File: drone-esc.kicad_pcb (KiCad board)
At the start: 4 copper layers, 30 x 30 mm, 0 parts

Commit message: added board footprint
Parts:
- added C1: 100n, Capacitor_SMD:C_0201_0603Metric, B.Cu at (140.5, 118.2)
- added C10: 10u, Capacitor_SMD:C_0805_2012Metric, B.Cu at (157.3, 124.8)
- added C11: 10u, Capacitor_SMD:C_0805_2012Metric, B.Cu at (157.3, 127.8)
- added C12: 10u, Capacitor_SMD:C_0805_2012Metric, B.Cu at (152.8, 118.8)
- added C13: 10u, Capacitor_SMD:C_0805_2012Metric, B.Cu at (152.8, 121.8)
- added C14: 10u, Capacitor_SMD:C_0805_2012Metric, B.Cu at (152.8, 124.8)
- added C15: 10u, Capacitor_SMD:C_0805_2012Metric, B.Cu at (152.8, 127.8)
- added C16: 10u, Capacitor_SMD:C_0805_2012Metric, B.Cu at (148.4, 118.8)
- added C17: 10u, Capacitor_SMD:C_0805_2012Metric, B.Cu at (148.4, 121.8)
- added C18: 10u, Capacitor_SMD:C_0805_2012Metric, B.Cu at (148.4, 124.8)
- added C19: 10u, Capacitor_SMD:C_0805_2012Metric, B.Cu at (148.4, 127.8)
- added C2: 100n, Capacitor_SMD:C_0201_0603Metric, B.Cu at (140.5, 119.9)
- added C20: 10u, Capacitor_SMD:C_0805_2012Metric, B.Cu at (143.9, 118.8)
- added C21: 10u, Capacitor_SMD:C_0805_2012Metric, B.Cu at (143.9, 121.8)
- added C22: 10u, Capacitor_SMD:C_0805_2012Metric, B.Cu at (143.9, 124.8)
- added C23: 10u, Capacitor_SMD:C_0805_2012Metric, B.Cu at (143.9, 127.8)
- added C25: 100n, Capacitor_SMD:C_0201_0603Metric, F.Cu at (104.3, 43.2)
- added C26: 100n, Capacitor_SMD:C_0201_0603Metric, F.Cu at (104.3, 45.0)
- added C27: 100n, Capacitor_SMD:C_0201_0603Metric, F.Cu at (104.3, 46.7)
- added C28: 100n, Capacitor_SMD:C_0201_0603Metric, F.Cu at (181.7, 42.9)
- added C29: 100n, Capacitor_SMD:C_0201_0603Metric, F.Cu at (104.3, 48.5)
- added C3: 1u, Capacitor_SMD:C_0201_0603Metric, B.Cu at (140.5, 121.7)
- added C30: 100n, Capacitor_SMD:C_0201_0603Metric, F.Cu at (104.3, 50.2)
- added C31: 100n, Capacitor_SMD:C_0201_0603Metric, F.Cu at (104.3, 52.0)
- added C32: 100n, Capacitor_SMD:C_0201_0603Metric, F.Cu at (104.3, 53.7)
- added C33: 100n, Capacitor_SMD:C_0201_0603Metric, F.Cu at (83.0, 111.8)
- added C34: 100n, Capacitor_SMD:C_0201_0603Metric, F.Cu at (83.0, 113.5)
- added C35: 100n, Capacitor_SMD:C_0201_0603Metric, F.Cu at (83.0, 115.3)
- added C36: 100n, Capacitor_SMD:C_0201_0603Metric, F.Cu at (83.0, 117.0)
- added C37: 100n, Capacitor_SMD:C_0201_0603Metric, F.Cu at (83.0, 118.8)
- added C38: 100n, Capacitor_SMD:C_0201_0603Metric, F.Cu at (83.0, 120.5)
- added C39: 100n, Capacitor_SMD:C_0201_0603Metric, F.Cu at (83.0, 122.3)
- added C4: 2u2, Capacitor_SMD:C_0201_0603Metric, B.Cu at (140.5, 123.4)
- added C40: 100n, Capacitor_SMD:C_0201_0603Metric, F.Cu at (83.0, 124.0)
- added C41: 100n, Capacitor_SMD:C_0201_0603Metric, F.Cu at (85.4, 111.8)
- added C42: 100n, Capacitor_SMD:C_0201_0603Metric, F.Cu at (104.3, 55.5)
- added C43: 100n, Capacitor_SMD:C_0201_0603Metric, F.Cu at (181.7, 44.6)
- added C44: 100n, Capacitor_SMD:C_0201_0603Metric, F.Cu at (181.7, 46.4)
- added C45: 100n, Capacitor_SMD:C_0201_0603Metric, F.Cu at (106.7, 43.2)
- added C46: 100n, Capacitor_SMD:C_0201_0603Metric, F.Cu at (181.7, 48.1)
- added C47: 100n, Capacitor_SMD:C_0201_0603Metric, F.Cu at (181.7, 49.9)
- added C48: 100n, Capacitor_SMD:C_0201_0603Metric, F.Cu at (181.7, 51.6)
- added C49: 100n, Capacitor_SMD:C_0201_0603Metric, F.Cu at (181.7, 53.4)
- added C5: 22u, Capacitor_SMD:C_0201_0603Metric, B.Cu at (138.0, 118.2)
- added C50: 100n, Capacitor_SMD:C_0201_0603Metric, F.Cu at (181.7, 55.1)
- added C51: 100n, Capacitor_SMD:C_0201_0603Metric, F.Cu at (184.2, 42.9)
- added C52: 100n, Capacitor_SMD:C_0201_0603Metric, F.Cu at (190.4, 111.1)
- added C53: 100n, Capacitor_SMD:C_0201_0603Metric, F.Cu at (190.4, 112.8)
- added C54: 100n, Capacitor_SMD:C_0201_0603Metric, F.Cu at (190.4, 114.6)
- added C55: 100n, Capacitor_SMD:C_0201_0603Metric, F.Cu at (190.4, 116.3)
- added C56: 100n, Capacitor_SMD:C_0201_0603Metric, F.Cu at (190.4, 118.1)
- added C57: 100n, Capacitor_SMD:C_0201_0603Metric, F.Cu at (190.4, 119.8)
- added C58: 100n, Capacitor_SMD:C_0201_0603Metric, F.Cu at (190.4, 121.6)
- added C59: 100n, Capacitor_SMD:C_0201_0603Metric, F.Cu at (190.4, 123.3)
- added C6: 10u, Capacitor_SMD:C_0201_0603Metric, B.Cu at (138.0, 119.9)
- added C60: 100n, Capacitor_SMD:C_0201_0603Metric, F.Cu at (192.9, 111.1)
- added C7: 22u, Capacitor_SMD:C_0201_0603Metric, B.Cu at (138.0, 121.7)
- added C8: 10u, Capacitor_SMD:C_0805_2012Metric, B.Cu at (157.3, 118.8)
- added C9: 10u, Capacitor_SMD:C_0805_2012Metric, B.Cu at (157.3, 121.8)
- added D1: SMF5.0A, Diode_SMD:D_SOD-123F, B.Cu at (141.9, 146.8)
- added D1: SMF5.0A, Diode_SMD:D_SOD-123F, B.Cu at (138.9, 126.0)
- added D2: HSMG-C170, LED_SMD:LED_0805_2012Metric, B.Cu at (136.3, 130.9)
- added D3: HSMD-C170, LED_SMD:LED_0805_2012Metric, B.Cu at (136.3, 133.9)
- added D4: HSMG-C170, LED_SMD:LED_0805_2012Metric, F.Cu at (114.4, 64.1)
- added D5: HSMG-C170, LED_SMD:LED_0805_2012Metric, F.Cu at (93.1, 132.7)
- added D6: HSMG-C170, LED_SMD:LED_0805_2012Metric, F.Cu at (191.9, 63.8)
- added D7: HSMG-C170, LED_SMD:LED_0805_2012Metric, F.Cu at (200.6, 132.0)
- added FB1: BLM03HD331SN1D, Resistor_SMD:R_0201_0603Metric, F.Cu at (106.7, 45.0)
- added FB2: BLM03HD331SN1D, Resistor_SMD:R_0201_0603Metric, F.Cu at (85.4, 113.5)
- added FB3: BLM03HD331SN1D, Resistor_SMD:R_0201_0603Metric, F.Cu at (184.2, 44.6)
- added FB4: BLM03HD331SN1D, Resistor_SMD:R_0201_0603Metric, F.Cu at (192.9, 112.8)
- added J1: SM08B-SRSS-TB_LF__SN_, SM08B-SRSS-TB:JST_SM08B-SRSS-TB_LF__SN_, B.Cu at (145.1, 80.2)
- added L1: 1u, Inductor_SMD:L_0603_1608Metric, B.Cu at (136.5, 136.7)
- added Q1: IRLHS6242, IRLHS6242TRPBF:IRL100HS121-V, F.Cu at (100.6, 44.6)
- added Q10: IRLHS6242, IRLHS6242TRPBF:IRL100HS121-V, F.Cu at (79.3, 127.1)
- added Q11: IRLHS6242, IRLHS6242TRPBF:IRL100HS121-V, F.Cu at (79.3, 131.7)
- added Q12: IRLHS6242, IRLHS6242TRPBF:IRL100HS121-V, F.Cu at (79.3, 136.3)
- added Q13: IRLHS6242, IRLHS6242TRPBF:IRL100HS121-V, F.Cu at (178.0, 44.3)
- added Q14: IRLHS6242, IRLHS6242TRPBF:IRL100HS121-V, F.Cu at (178.0, 49.0)
- added Q15: IRLHS6242, IRLHS6242TRPBF:IRL100HS121-V, F.Cu at (178.0, 53.6)
- added Q16: IRLHS6242, IRLHS6242TRPBF:IRL100HS121-V, F.Cu at (178.0, 58.2)
- added Q17: IRLHS6242, IRLHS6242TRPBF:IRL100HS121-V, F.Cu at (178.0, 62.8)
- added Q18: IRLHS6242, IRLHS6242TRPBF:IRL100HS121-V, F.Cu at (178.0, 67.4)
- added Q19: IRLHS6242, IRLHS6242TRPBF:IRL100HS121-V, F.Cu at (186.7, 112.5)
- added Q2: IRLHS6242, IRLHS6242TRPBF:IRL100HS121-V, F.Cu at (100.6, 49.3)
- added Q20: IRLHS6242, IRLHS6242TRPBF:IRL100HS121-V, F.Cu at (186.7, 117.2)
- added Q21: IRLHS6242, IRLHS6242TRPBF:IRL100HS121-V, F.Cu at (186.7, 121.8)
- added Q22: IRLHS6242, IRLHS6242TRPBF:IRL100HS121-V, F.Cu at (186.7, 126.4)
- added Q23: IRLHS6242, IRLHS6242TRPBF:IRL100HS121-V, F.Cu at (186.7, 131.0)
- added Q24: IRLHS6242, IRLHS6242TRPBF:IRL100HS121-V, F.Cu at (186.7, 135.6)
- added Q3: IRLHS6242, IRLHS6242TRPBF:IRL100HS121-V, F.Cu at (100.6, 53.9)
- added Q4: IRLHS6242, IRLHS6242TRPBF:IRL100HS121-V, F.Cu at (100.6, 58.5)
- added Q5: IRLHS6242, IRLHS6242TRPBF:IRL100HS121-V, F.Cu at (100.6, 63.1)
- added Q6: IRLHS6242, IRLHS6242TRPBF:IRL100HS121-V, F.Cu at (100.6, 67.7)
- added Q7: IRLHS6242, IRLHS6242TRPBF:IRL100HS121-V, F.Cu at (79.3, 113.2)
- added Q8: IRLHS6242, IRLHS6242TRPBF:IRL100HS121-V, F.Cu at (79.3, 117.9)
- added Q9: IRLHS6242, IRLHS6242TRPBF:IRL100HS121-V, F.Cu at (79.3, 122.5)
- added R1: 1m, Resistor_SMD:R_2512_6332Metric, B.Cu at (142.9, 131.8)
- added R10: 100k, Resistor_SMD:R_0201_0603Metric, F.Cu at (106.7, 53.7)
- added R11: 100k, Resistor_SMD:R_0201_0603Metric, F.Cu at (184.2, 46.4)
- added R12: 15R, Resistor_SMD:R_0201_0603Metric, F.Cu at (106.7, 55.5)
- added R13: 15R, Resistor_SMD:R_0201_0603Metric, F.Cu at (109.2, 43.2)
- added R14: 15R, Resistor_SMD:R_0201_0603Metric, F.Cu at (109.2, 45.0)
- added R15: 15R, Resistor_SMD:R_0201_0603Metric, F.Cu at (109.2, 46.7)
- added R16: 15R, Resistor_SMD:R_0201_0603Metric, F.Cu at (109.2, 48.5)
- added R17: 4.7k, Resistor_SMD:R_0201_0603Metric, F.Cu at (109.2, 50.2)
- added R18: 1k, Resistor_SMD:R_0201_0603Metric, F.Cu at (109.2, 52.0)
- added R19: 10k, Resistor_SMD:R_0201_0603Metric, F.Cu at (109.2, 53.7)
- added R2: 1k, Resistor_SMD:R_0201_0603Metric, B.Cu at (142.9, 136.7)
- added R20: 4.7k, Resistor_SMD:R_0201_0603Metric, F.Cu at (109.2, 55.5)
- added R21: 10k, Resistor_SMD:R_0201_0603Metric, F.Cu at (111.6, 43.2)
- added R22: 1k, Resistor_SMD:R_0201_0603Metric, F.Cu at (111.6, 45.0)
- added R23: 4.7k, Resistor_SMD:R_0201_0603Metric, F.Cu at (111.6, 46.7)
- added R24: 10k, Resistor_SMD:R_0201_0603Metric, F.Cu at (111.6, 48.5)
- added R25: 1k, Resistor_SMD:R_0201_0603Metric, F.Cu at (111.6, 50.2)
- added R26: 10k, Resistor_SMD:R_0201_0603Metric, F.Cu at (85.4, 115.3)
- added R27: 100k, Resistor_SMD:R_0201_0603Metric, F.Cu at (85.4, 117.0)
- added R28: 100k, Resistor_SMD:R_0201_0603Metric, F.Cu at (85.4, 118.8)
- added R29: 100k, Resistor_SMD:R_0201_0603Metric, F.Cu at (85.4, 120.5)
- added R3: 732k, Resistor_SMD:R_0201_0603Metric, B.Cu at (138.0, 123.4)
- added R30: 10k, Resistor_SMD:R_0201_0603Metric, F.Cu at (85.4, 122.3)
- added R31: 220R, Resistor_SMD:R_0201_0603Metric, F.Cu at (85.4, 124.0)
- added R32: 15R, Resistor_SMD:R_0201_0603Metric, F.Cu at (87.9, 111.8)
- added R33: 15R, Resistor_SMD:R_0201_0603Metric, F.Cu at (87.9, 113.5)
- added R34: 4.7k, Resistor_SMD:R_0201_0603Metric, F.Cu at (87.9, 115.3)
- added R35: 10k, Resistor_SMD:R_0201_0603Metric, F.Cu at (87.9, 117.0)
- added R36: 15R, Resistor_SMD:R_0201_0603Metric, F.Cu at (87.9, 118.8)
- added R37: 15R, Resistor_SMD:R_0201_0603Metric, F.Cu at (87.9, 120.5)
- added R38: 1k, Resistor_SMD:R_0201_0603Metric, F.Cu at (87.9, 122.3)
- added R39: 4.7k, Resistor_SMD:R_0201_0603Metric, F.Cu at (87.9, 124.0)
- added R4: 100k, Resistor_SMD:R_0201_0603Metric, B.Cu at (135.6, 118.2)
- added R40: 10k, Resistor_SMD:R_0201_0603Metric, F.Cu at (90.3, 111.8)
- added R41: 1k, Resistor_SMD:R_0201_0603Metric, F.Cu at (90.3, 113.5)
- added R42: 15R, Resistor_SMD:R_0201_0603Metric, F.Cu at (90.3, 115.3)
- added R43: 15R, Resistor_SMD:R_0201_0603Metric, F.Cu at (90.3, 117.0)
- added R44: 4.7k, Resistor_SMD:R_0201_0603Metric, F.Cu at (90.3, 118.8)
- added R45: 10k, Resistor_SMD:R_0201_0603Metric, F.Cu at (90.3, 120.5)
- added R46: 1k, Resistor_SMD:R_0201_0603Metric, F.Cu at (90.3, 122.3)
- added R47: 10k, Resistor_SMD:R_0201_0603Metric, F.Cu at (111.6, 52.0)
- added R48: 10k, Resistor_SMD:R_0201_0603Metric, F.Cu at (184.2, 48.1)
- added R49: 100k, Resistor_SMD:R_0201_0603Metric, F.Cu at (184.2, 49.9)
- added R5: 360, Resistor_SMD:R_0201_0603Metric, B.Cu at (135.6, 119.9)
- added R50: 100k, Resistor_SMD:R_0201_0603Metric, F.Cu at (184.2, 51.6)
- added R51: 10k, Resistor_SMD:R_0201_0603Metric, F.Cu at (184.2, 53.4)
- added R52: 220R, Resistor_SMD:R_0201_0603Metric, F.Cu at (184.2, 55.1)
- added R53: 15R, Resistor_SMD:R_0201_0603Metric, F.Cu at (111.6, 53.7)
- added R54: 15R, Resistor_SMD:R_0201_0603Metric, F.Cu at (186.6, 42.9)
- added R55: 15R, Resistor_SMD:R_0201_0603Metric, F.Cu at (186.6, 44.6)
- added R56: 4.7k, Resistor_SMD:R_0201_0603Metric, F.Cu at (186.6, 46.4)
- added R57: 10k, Resistor_SMD:R_0201_0603Metric, F.Cu at (186.6, 48.1)
- added R58: 15R, Resistor_SMD:R_0201_0603Metric, F.Cu at (186.6, 49.9)
- added R59: 15R, Resistor_SMD:R_0201_0603Metric, F.Cu at (186.6, 51.6)
- added R6: 10k, Resistor_SMD:R_0201_0603Metric, F.Cu at (106.7, 46.7)
- added R60: 1k, Resistor_SMD:R_0201_0603Metric, F.Cu at (186.6, 53.4)
- added R61: 4.7k, Resistor_SMD:R_0201_0603Metric, F.Cu at (186.6, 55.1)
- added R62: 10k, Resistor_SMD:R_0201_0603Metric, F.Cu at (189.1, 42.9)
- added R63: 1k, Resistor_SMD:R_0201_0603Metric, F.Cu at (189.1, 44.6)
- added R64: 15R, Resistor_SMD:R_0201_0603Metric, F.Cu at (189.1, 46.4)
- added R65: 15R, Resistor_SMD:R_0201_0603Metric, F.Cu at (189.1, 48.1)
- added R66: 4.7k, Resistor_SMD:R_0201_0603Metric, F.Cu at (189.1, 49.9)
- added R67: 10k, Resistor_SMD:R_0201_0603Metric, F.Cu at (189.1, 51.6)
- added R68: 1k, Resistor_SMD:R_0201_0603Metric, F.Cu at (189.1, 53.4)
- added R69: 10k, Resistor_SMD:R_0201_0603Metric, F.Cu at (192.9, 114.6)
- added R7: 220R, Resistor_SMD:R_0201_0603Metric, F.Cu at (106.7, 48.5)
- added R70: 100k, Resistor_SMD:R_0201_0603Metric, F.Cu at (192.9, 116.3)
- added R71: 100k, Resistor_SMD:R_0201_0603Metric, F.Cu at (192.9, 118.1)
- added R72: 100k, Resistor_SMD:R_0201_0603Metric, F.Cu at (192.9, 119.8)
- added R73: 10k, Resistor_SMD:R_0201_0603Metric, F.Cu at (192.9, 121.6)
- added R74: 220R, Resistor_SMD:R_0201_0603Metric, F.Cu at (192.9, 123.3)
- added R75: 15R, Resistor_SMD:R_0201_0603Metric, F.Cu at (195.3, 111.1)
- added R76: 15R, Resistor_SMD:R_0201_0603Metric, F.Cu at (195.3, 112.8)
- added R77: 4.7k, Resistor_SMD:R_0201_0603Metric, F.Cu at (195.3, 114.6)
- added R78: 10k, Resistor_SMD:R_0201_0603Metric, F.Cu at (195.3, 116.3)
- added R79: 15R, Resistor_SMD:R_0201_0603Metric, F.Cu at (195.3, 118.1)
- added R8: 100k, Resistor_SMD:R_0201_0603Metric, F.Cu at (106.7, 50.2)
- added R80: 15R, Resistor_SMD:R_0201_0603Metric, F.Cu at (195.3, 119.8)
- added R81: 1k, Resistor_SMD:R_0201_0603Metric, F.Cu at (195.3, 121.6)
- added R82: 4.7k, Resistor_SMD:R_0201_0603Metric, F.Cu at (195.3, 123.3)
- added R83: 10k, Resistor_SMD:R_0201_0603Metric, F.Cu at (197.8, 111.1)
- added R84: 1k, Resistor_SMD:R_0201_0603Metric, F.Cu at (197.8, 112.8)
- added R85: 15R, Resistor_SMD:R_0201_0603Metric, F.Cu at (197.8, 114.6)
- added R86: 15R, Resistor_SMD:R_0201_0603Metric, F.Cu at (197.8, 116.3)
- added R87: 4.7k, Resistor_SMD:R_0201_0603Metric, F.Cu at (197.8, 118.1)
- added R88: 10k, Resistor_SMD:R_0201_0603Metric, F.Cu at (197.8, 119.8)
- added R89: 1k, Resistor_SMD:R_0201_0603Metric, F.Cu at (197.8, 121.6)
- added R9: 100k, Resistor_SMD:R_0201_0603Metric, F.Cu at (106.7, 52.0)
- added R90: 900, Resistor_SMD:R_0201_0603Metric, B.Cu at (135.6, 121.7)
- added R91: 360, Resistor_SMD:R_0201_0603Metric, F.Cu at (111.6, 55.5)
- added R92: 360, Resistor_SMD:R_0201_0603Metric, F.Cu at (90.3, 124.0)
- added R93: 360, Resistor_SMD:R_0201_0603Metric, F.Cu at (189.1, 55.1)
- added R94: 360, Resistor_SMD:R_0201_0603Metric, F.Cu at (197.8, 123.3)
- added TP10: SWDIO, TestPoint:TestPoint_Pad_D1.0mm, F.Cu at (182.0, 63.6)
- added TP11: NRST, TestPoint:TestPoint_Pad_D1.0mm, F.Cu at (190.7, 125.8)
- added TP12: SWCLK, TestPoint:TestPoint_Pad_D1.0mm, F.Cu at (190.7, 128.8)
- added TP13: SWDIO, TestPoint:TestPoint_Pad_D1.0mm, F.Cu at (190.7, 131.8)
- added TP14: BATT, TestPoint:TestPoint_Pad_D1.0mm, B.Cu at (158.0, 136.1)
- added TP15: GND, TestPoint:TestPoint_Pad_D1.0mm, B.Cu at (158.0, 141.0)
- added TP16: 3V3, TestPoint:TestPoint_Pad_D1.0mm, B.Cu at (154.9, 136.1)
- added TP17: 5V, TestPoint:TestPoint_Pad_D1.0mm, B.Cu at (154.9, 141.0)
- added TP18: CURR, TestPoint:TestPoint_Pad_D1.0mm, B.Cu at (151.9, 136.1)
- added TP19: BOOT0, TestPoint:TestPoint_Pad_D1.0mm, F.Cu at (107.6, 57.9)
- added TP2: SWCLK, TestPoint:TestPoint_Pad_D1.0mm, F.Cu at (104.6, 57.9)
- added TP20: BOOT0, TestPoint:TestPoint_Pad_D1.0mm, F.Cu at (86.3, 126.5)
- added TP21: BOOT0, TestPoint:TestPoint_Pad_D1.0mm, F.Cu at (185.1, 57.5)
- added TP22: BOOT0, TestPoint:TestPoint_Pad_D1.0mm, F.Cu at (193.8, 125.8)
- added TP23: GND, TestPoint:TestPoint_Pad_D1.0mm, B.Cu at (151.9, 141.0)
- added TP24: GAH, TestPoint:TestPoint_Pad_D1.0mm, F.Cu at (107.6, 60.9)
- added TP25: GAH, TestPoint:TestPoint_Pad_D1.0mm, F.Cu at (86.3, 129.5)
- added TP26: GAH, TestPoint:TestPoint_Pad_D1.0mm, F.Cu at (185.1, 60.6)
- added TP27: GAH, TestPoint:TestPoint_Pad_D1.0mm, F.Cu at (193.8, 128.8)
- added TP3: NRST, TestPoint:TestPoint_Pad_D1.0mm, F.Cu at (104.6, 60.9)
- added TP36: GAL, TestPoint:TestPoint_Pad_D1.0mm, F.Cu at (107.6, 64.0)
- added TP37: GAL, TestPoint:TestPoint_Pad_D1.0mm, F.Cu at (86.3, 132.6)
- added TP38: GAL, TestPoint:TestPoint_Pad_D1.0mm, F.Cu at (185.1, 63.6)
- added TP39: GAL, TestPoint:TestPoint_Pad_D1.0mm, F.Cu at (193.8, 131.8)
- added TP4: NRST, TestPoint:TestPoint_Pad_D1.0mm, F.Cu at (83.3, 126.5)
- added TP48: MOTORA, TestPoint:TestPoint_Pad_D1.0mm, F.Cu at (110.7, 57.9)
- added TP49: MOTORA, TestPoint:TestPoint_Pad_D1.0mm, F.Cu at (89.4, 126.5)
- added TP5: SWCLK, TestPoint:TestPoint_Pad_D1.0mm, F.Cu at (83.3, 129.5)
- added TP50: MOTORA, TestPoint:TestPoint_Pad_D1.0mm, F.Cu at (188.1, 57.5)
- added TP51: MOTORA, TestPoint:TestPoint_Pad_D1.0mm, F.Cu at (196.8, 125.8)
- added TP52: MOTORB, TestPoint:TestPoint_Pad_D1.0mm, F.Cu at (110.7, 60.9)
- added TP53: MOTORB, TestPoint:TestPoint_Pad_D1.0mm, F.Cu at (89.4, 129.5)
- added TP54: MOTORB, TestPoint:TestPoint_Pad_D1.0mm, F.Cu at (188.1, 60.6)
- added TP55: MOTORB, TestPoint:TestPoint_Pad_D1.0mm, F.Cu at (196.8, 128.8)
- added TP56: MOTORC, TestPoint:TestPoint_Pad_D1.0mm, F.Cu at (110.7, 64.0)
- added TP57: MOTORC, TestPoint:TestPoint_Pad_D1.0mm, F.Cu at (89.4, 132.6)
- added TP58: MOTORC, TestPoint:TestPoint_Pad_D1.0mm, F.Cu at (188.1, 63.6)
- added TP59: MOTORC, TestPoint:TestPoint_Pad_D1.0mm, F.Cu at (196.8, 131.8)
- added TP6: SWDIO, TestPoint:TestPoint_Pad_D1.0mm, F.Cu at (83.3, 132.6)
- added TP7: NRST, TestPoint:TestPoint_Pad_D1.0mm, F.Cu at (182.0, 57.5)
- added TP8: SWCLK, TestPoint:TestPoint_Pad_D1.0mm, F.Cu at (182.0, 60.6)
- added TP9: SWDIO, TestPoint:TestPoint_Pad_D1.0mm, F.Cu at (104.6, 64.0)
- added U1: ~, esc-board-copper:esc-board, F.Cu at (145.0, 95.0)
- added U10: DGD05473FNQ-7, Package_DFN_QFN:DFN-10-1EP_3x3mm_P0.5mm_EP1.7x2.5mm, F.Cu at (94.6, 117.8)
- added U11: DGD05473FNQ-7, Package_DFN_QFN:DFN-10-1EP_3x3mm_P0.5mm_EP1.7x2.5mm, F.Cu at (94.6, 122.3)
- added U12: AT32F421G8U7, Package_DFN_QFN:QFN-28-1EP_4x4mm_P0.45mm_EP2.4x2.4mm, F.Cu at (94.4, 128.1)
- added U13: DGD05473FNQ-7, Package_DFN_QFN:DFN-10-1EP_3x3mm_P0.5mm_EP1.7x2.5mm, F.Cu at (193.3, 44.3)
- added U14: DGD05473FNQ-7, Package_DFN_QFN:DFN-10-1EP_3x3mm_P0.5mm_EP1.7x2.5mm, F.Cu at (193.3, 48.9)
- added U15: DGD05473FNQ-7, Package_DFN_QFN:DFN-10-1EP_3x3mm_P0.5mm_EP1.7x2.5mm, F.Cu at (193.3, 53.4)
- added U16: AT32F421G8U7, Package_DFN_QFN:QFN-28-1EP_4x4mm_P0.45mm_EP2.4x2.4mm, F.Cu at (193.1, 59.1)
- added U17: DGD05473FNQ-7, Package_DFN_QFN:DFN-10-1EP_3x3mm_P0.5mm_EP1.7x2.5mm, F.Cu at (202.0, 112.5)
- added U18: DGD05473FNQ-7, Package_DFN_QFN:DFN-10-1EP_3x3mm_P0.5mm_EP1.7x2.5mm, F.Cu at (202.0, 117.0)
- added U19: DGD05473FNQ-7, Package_DFN_QFN:DFN-10-1EP_3x3mm_P0.5mm_EP1.7x2.5mm, F.Cu at (202.0, 121.6)
- added U2: INA186A3IDCKR, INA186A3IDCKR:SOT65P210X110-6N, B.Cu at (144.4, 140.9)
- added U20: AT32F421G8U7, Package_DFN_QFN:QFN-28-1EP_4x4mm_P0.45mm_EP2.4x2.4mm, F.Cu at (201.8, 127.3)
- added U3: TLV76733DRVR, Package_SON:WSON-6-1EP_2x2mm_P0.65mm_EP1x1.6mm_ThermalVias, B.Cu at (136.7, 139.8)
- added U4: TPS61023DRLR, TPS61023DRLR:DRL0006A, B.Cu at (139.8, 139.5)
- added U5: AT32F421G8U7, Package_DFN_QFN:QFN-28-1EP_4x4mm_P0.45mm_EP2.4x2.4mm, F.Cu at (115.7, 59.5)
- added U6: DGD05473FNQ-7, Package_DFN_QFN:DFN-10-1EP_3x3mm_P0.5mm_EP1.7x2.5mm, F.Cu at (115.9, 44.6)
- added U7: DGD05473FNQ-7, Package_DFN_QFN:DFN-10-1EP_3x3mm_P0.5mm_EP1.7x2.5mm, F.Cu at (115.9, 49.1)
- added U8: DGD05473FNQ-7, Package_DFN_QFN:DFN-10-1EP_3x3mm_P0.5mm_EP1.7x2.5mm, F.Cu at (115.9, 53.7)
- added U9: DGD05473FNQ-7, Package_DFN_QFN:DFN-10-1EP_3x3mm_P0.5mm_EP1.7x2.5mm, F.Cu at (94.6, 113.2)
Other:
- outline, holes or cut-outs redrawn

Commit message: basic placement 1
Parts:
- removed C11, C15, C20, C23: 10u, Capacitor_SMD:C_0805_2012Metric
- C10, C12, C13, C14, C16, C17, C18, C19, C21, C22, C8, C9: moved to F.Cu
- C29, C31, C42, C45, FB1, R10, R12, R13, R14, R15, R16, R17, R18, R19, R20, R21, R22, R23, R24, R25, R47, R53, R6, R7, R8, R9, R91, TP19, TP2, TP3, TP56, TP9, U5: moved to B.Cu
- moved C22 63.6 mm to (184.5, 75.9), turned to 90 degrees
- moved C19 61.1 mm to (180.5, 75.9), turned to 90 degrees
- moved C21 60.0 mm to (182.5, 75.9), turned to 90 degrees
- moved C18 58.1 mm to (184.5, 79.3), turned to 90 degrees
- moved C17 54.5 mm to (182.5, 79.3), turned to 90 degrees
- moved C14 52.7 mm to (184.5, 82.7), turned to 90 degrees
- moved C16 50.9 mm to (180.5, 79.3), turned to 90 degrees
- moved C13 49.1 mm to (182.5, 82.7), turned to 90 degrees
- moved C10 47.3 mm to (184.5, 86.1), turned to 90 degrees
- moved C12 45.5 mm to (180.5, 82.7), turned to 90 degrees
- moved C9 43.7 mm to (182.5, 86.1), turned to 90 degrees
- moved C8 40.1 mm to (180.5, 86.1), turned to 90 degrees
- moved D4 37.2 mm to (140.1, 37.1), turned to 90 degrees
- moved TP24 35.4 mm to (83.5, 35.0)
- moved TP36 35.0 mm to (82.6, 39.4)
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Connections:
- J1 pad P1: (no net) -> GND
- J1 pad P2: (no net) -> GND
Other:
- board size 30 x 30 mm -> 34 x 34 mm

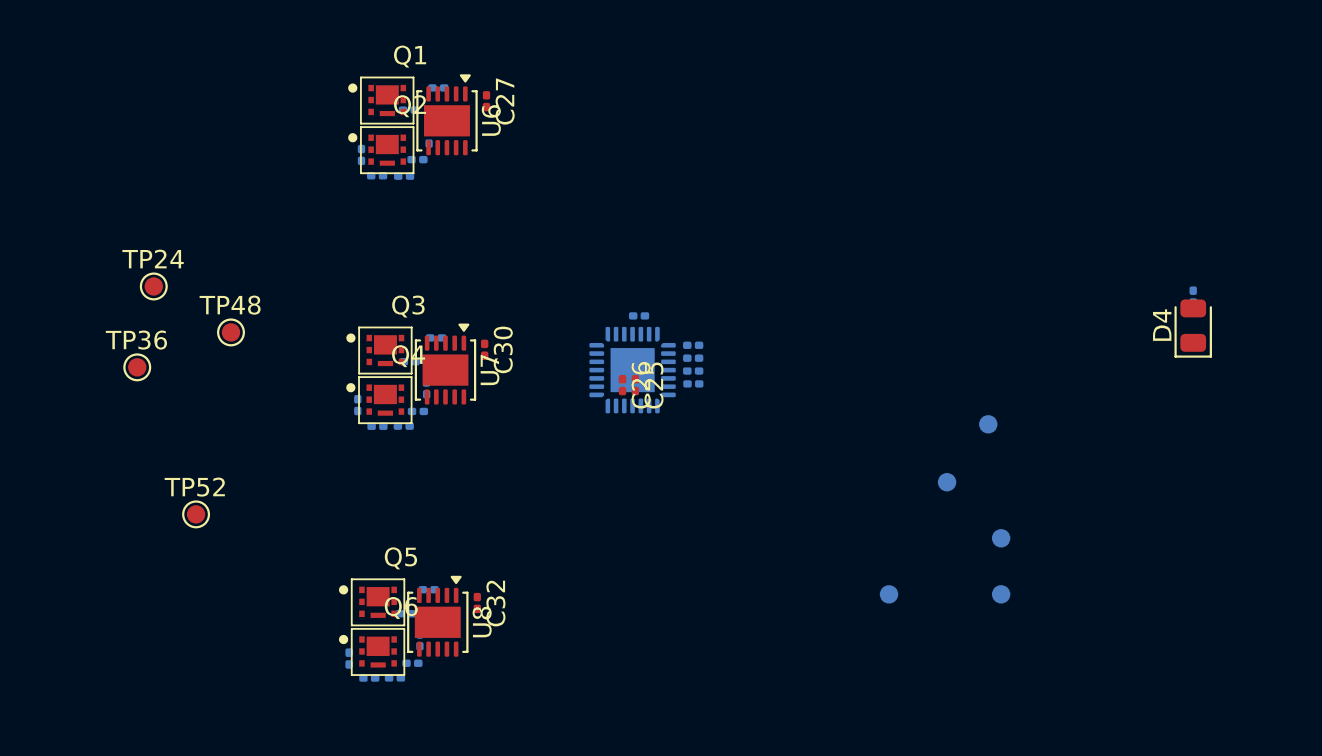
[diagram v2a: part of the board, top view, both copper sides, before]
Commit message: placement 2 (starting routing)
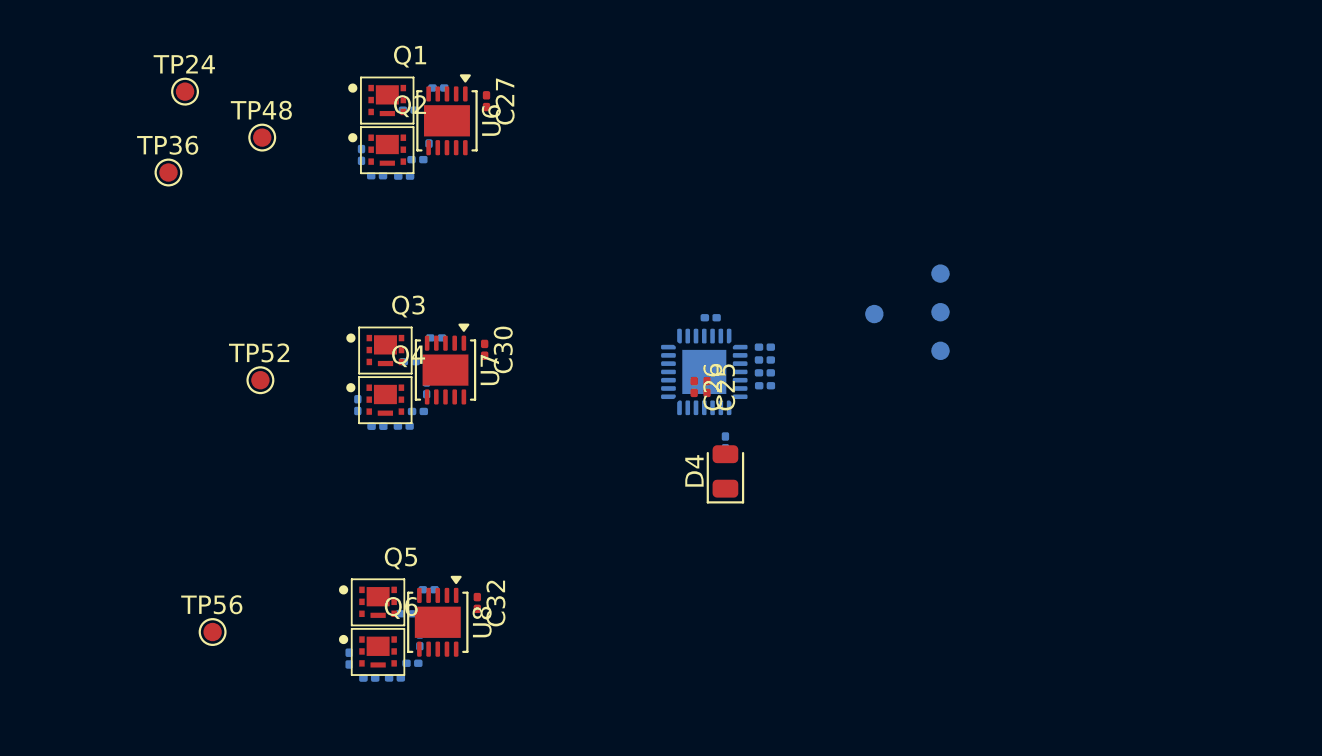
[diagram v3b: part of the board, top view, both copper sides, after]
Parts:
- TP56: moved to F.Cu
- moved TP56 36.9 mm to (86.7, 53.8), turned to 0 degrees
- moved R91 26.7 mm to (114.6, 43.5)
- moved D4 26.7 mm to (114.6, 45.1)
- moved TP9 17.8 mm to (126.3, 34.3)
- moved TP24 10.7 mm to (85.2, 24.4)
- moved TP48 10.7 mm to (89.4, 26.9)
- moved TP36 10.7 mm to (84.3, 28.8)
- moved TP3 10.7 mm to (126.3, 38.5)
- moved TP19 9.97 mm to (122.7, 36.5)
- moved TP52 8.10 mm to (89.3, 40.1)
- moved TP2 6.63 mm to (126.3, 36.4)
- moved C26 3.90 mm to (112.9, 40.5)
- moved C45 3.90 mm to (116.7, 39.7)
- moved R47 3.90 mm to (116.7, 39.0)
- moved R6 3.90 mm to (116.7, 38.3)
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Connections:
- U12 pad 10: /ESC2/FBB -> /ESC2/FBC
- U12 pad 11: /ESC2/FBC -> /ESC2/FBB
- U12 pad 14: /ESC2/B_LOW -> /ESC2/C_HIGH
- U12 pad 15: /ESC2/A_LOW -> /ESC2/B_LOW
- U12 pad 18: /ESC2/C_HIGH -> /ESC2/B_HIGH
- U12 pad 19: /ESC2/B_HIGH -> /ESC2/A_LOW
- U12 pad 23: unconnected-(U12-PA15-Pad23) -> /ESC2/ESC_EN
- U12 pad 24: unconnected-(U12-PB3-Pad24) -> /ESC2/FBA
- U12 pad 28: /ESC2/ESC_EN -> unconnected-(U12-PB7-Pad28)
- U12 pad 6: /ESC2/FBA -> unconnected-(U12-PA0-Pad6)
- U16 pad 10: /ESC3/FBB -> /ESC3/FBC
- U16 pad 11: /ESC3/FBC -> /ESC3/FBB
- U16 pad 14: /ESC3/B_LOW -> /ESC3/C_HIGH
- U16 pad 15: /ESC3/A_LOW -> /ESC3/B_LOW
- U16 pad 18: /ESC3/C_HIGH -> /ESC3/B_HIGH
- U16 pad 19: /ESC3/B_HIGH -> /ESC3/A_LOW
- U16 pad 23: unconnected-(U16-PA15-Pad23) -> /ESC3/ESC_EN
- U16 pad 24: unconnected-(U16-PB3-Pad24) -> /ESC3/FBA
- U16 pad 28: /ESC3/ESC_EN -> unconnected-(U16-PB7-Pad28)
- U16 pad 6: /ESC3/FBA -> unconnected-(U16-PA0-Pad6)
- U20 pad 10: /ESC4/FBB -> /ESC4/FBC
- U20 pad 11: /ESC4/FBC -> /ESC4/FBB
- U20 pad 14: /ESC4/B_LOW -> /ESC4/C_HIGH
- U20 pad 15: /ESC4/A_LOW -> /ESC4/B_LOW
- U20 pad 18: /ESC4/C_HIGH -> /ESC4/B_HIGH
- U20 pad 19: /ESC4/B_HIGH -> /ESC4/A_LOW
- U20 pad 23: unconnected-(U20-PA15-Pad23) -> /ESC4/ESC_EN
- U20 pad 24: unconnected-(U20-PB3-Pad24) -> /ESC4/FBA
- U20 pad 28: /ESC4/ESC_EN -> unconnected-(U20-PB7-Pad28)
- U20 pad 6: /ESC4/FBA -> unconnected-(U20-PA0-Pad6)
- U5 pad 10: /ESC1/FBB -> /ESC1/FBC
- U5 pad 11: /ESC1/FBC -> /ESC1/FBB
- U5 pad 14: /ESC1/B_LOW -> /ESC1/C_HIGH
- U5 pad 15: /ESC1/A_LOW -> /ESC1/B_LOW
- U5 pad 18: /ESC1/C_HIGH -> /ESC1/B_HIGH
- U5 pad 19: /ESC1/B_HIGH -> /ESC1/A_LOW
- U5 pad 23: unconnected-(U5-PA15-Pad23) -> /ESC1/ESC_EN
- U5 pad 24: unconnected-(U5-PB3-Pad24) -> /ESC1/FBA
- U5 pad 28: /ESC1/ESC_EN -> unconnected-(U5-PB7-Pad28)
- U5 pad 6: /ESC1/FBA -> unconnected-(U5-PA0-Pad6)

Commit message: placement of power
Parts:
- moved TP23 35.3 mm to (116.6, 141.1)
- moved TP15 35.3 mm to (122.7, 141.1)
- moved TP14 33.0 mm to (125.9, 128.4)
- moved R4 26.9 mm to (144.7, 143.4), turned to 90 degrees
- moved C5 26.2 mm to (139.3, 144.3), turned to -90 degrees
- moved C6 25.5 mm to (143.7, 144.8), turned to 0 degrees
- moved D1 24.7 mm to (131.6, 124.3)
- moved C7 22.7 mm to (138.1, 144.3), turned to -90 degrees
- moved R90 21.3 mm to (128.5, 141.8), turned to 0 degrees
- moved R3 20.7 mm to (143.4, 143.4), turned to -90 degrees
- moved R5 20.1 mm to (128.5, 138.7), turned to 0 degrees
- moved TP17 15.3 mm to (139.6, 141.9)
- moved C3 15.1 mm to (139.3, 136.7), turned to 90 degrees
- moved C4 13.5 mm to (142.7, 136.7), turned to -90 degrees
- moved C1 13.5 mm to (147.4, 129.8), turned to 90 degrees
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
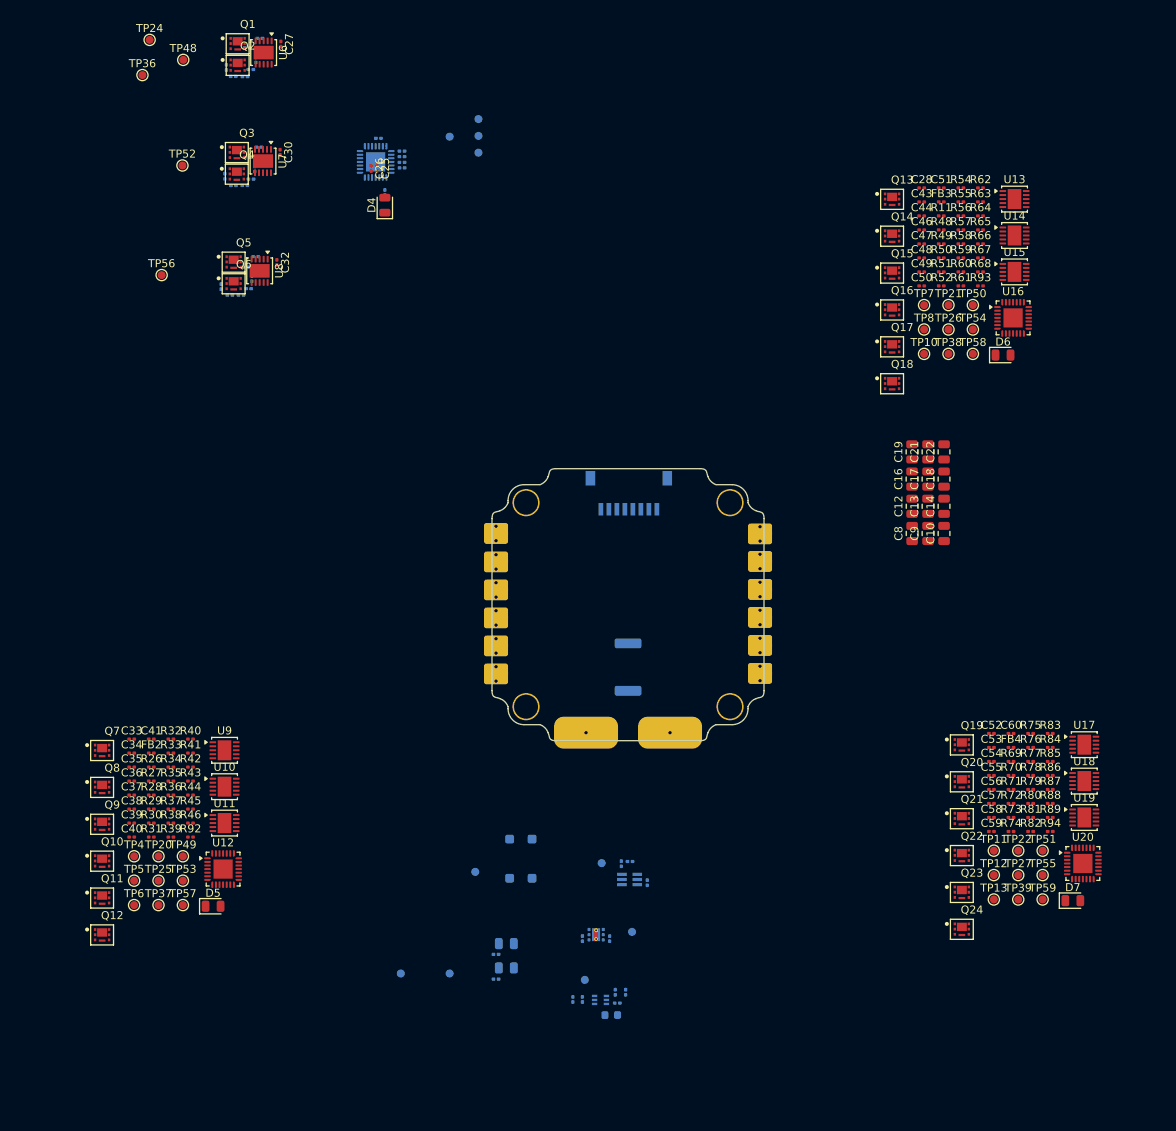
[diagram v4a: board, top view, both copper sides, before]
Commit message: esc1 place and route
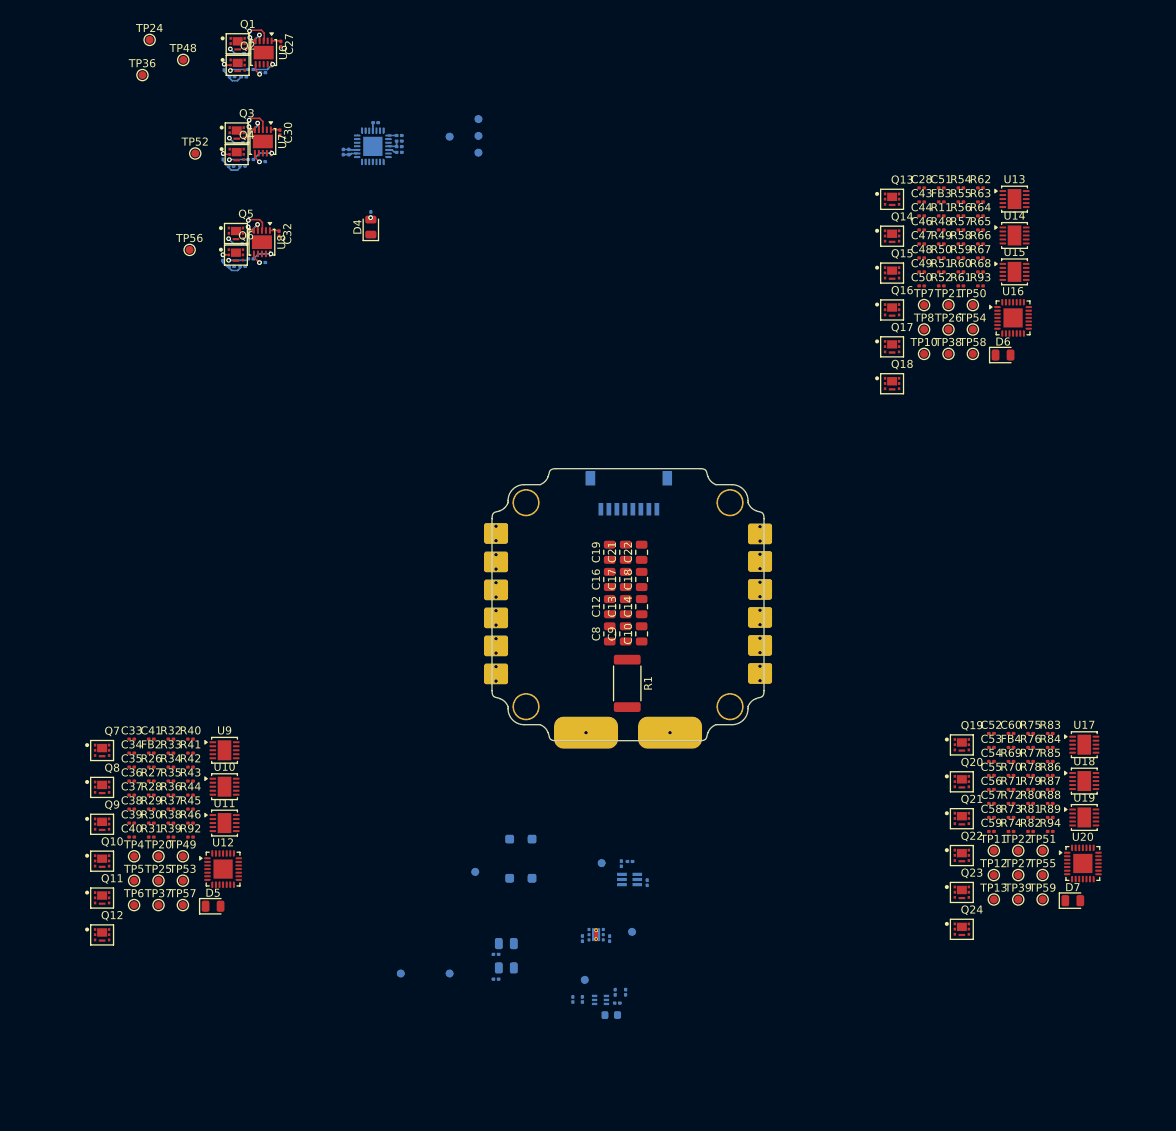
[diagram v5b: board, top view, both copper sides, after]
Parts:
- C25, C26: moved to B.Cu
- R1: moved to F.Cu
- moved C10 39.8 mm to (146.7, 98.7)
- moved C9 39.8 mm to (144.7, 98.7)
- moved C13 39.8 mm to (144.7, 95.2)
- moved C14 39.8 mm to (146.7, 95.2)
- moved C16 39.8 mm to (142.7, 91.8)
- moved C17 39.8 mm to (144.7, 91.8)
- moved C18 39.8 mm to (146.7, 91.8)
- moved C19 39.8 mm to (142.7, 88.5)
- moved C21 39.8 mm to (144.7, 88.5)
- moved C22 39.8 mm to (146.7, 88.5)
- moved C12 39.8 mm to (142.7, 95.2)
- moved C8 39.8 mm to (142.7, 98.7)
- moved TP56 4.71 mm to (90.2, 50.6)
- moved C25 4.67 mm to (109.4, 38.4)
- moved C31 4.23 mm to (97.5, 47.4), turned to -90 degrees
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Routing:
- net /ESC1/ESC_EN: track 0.00 -> 4.16 mm, vias 0 -> 3
- net /ESC1/GATE_B_HIGH: track 0.00 -> 3.87 mm, vias 0 -> 1
- net /ESC1/GATE_C_HIGH: track 0.00 -> 3.71 mm, vias 0 -> 1
- net /ESC1/MotorA: track 0.00 -> 3.63 mm, vias 0 -> 2
- net /ESC1/GATE_A_HIGH: track 0.00 -> 3.58 mm, vias 0 -> 1
- net /ESC1/MotorB: track 0.00 -> 3.58 mm, vias 0 -> 2
- net +5V: track 0.00 -> 3.52 mm
- net /ESC1/FBC: track 0.00 -> 3.24 mm
- net /ESC1/FBB: track 0.00 -> 3.19 mm
- net /ESC1/FBA: track 0.00 -> 3.08 mm
- net Net-(U6-VB): track 0.00 -> 3.04 mm, vias 0 -> 1
- net Net-(U7-VB): track 0.00 -> 3.01 mm, vias 0 -> 1
- net Net-(U8-VB): track 0.00 -> 2.96 mm, vias 0 -> 1
- net /ESC1/GATE_A_LOW: track 0.00 -> 2.68 mm, vias 0 -> 1
- net /ESC1/GATE_B_LOW: track 0.00 -> 2.63 mm, vias 0 -> 1
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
